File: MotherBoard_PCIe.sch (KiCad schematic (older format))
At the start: 27 parts, among them J1 Conn_01x04, J2 Conn_01x07, J3 Conn_01x04, J4 Conn_01x07, J5 Bus_PCIexpress_x16_164_Positi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, J6 Bus_PCIexpress_x16_164_Positi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, J7 Bus_PCIexpress_x16_164_Positi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

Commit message: buck-up
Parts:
- removed C1: 10uF, Capacitor_SMD:C_1206_3216Metric, symbol Device:C
- removed C10: 1000uF, Capacitor_THT:CP_Radial_D12.5mm_P5.00mm, symbol Device:CP
- removed H5, H6: MountingHole, MountingHole:MountingHole_3.2mm_M3, symbol Mechanical:MountingHole
- removed J1, J3: Conn_01x04, Connector_PinSocket_2.54mm:PinSocket_1x04_P2.54mm_Vertical, symbol Connector_Generic:Conn_01x04
- added C1, C?: 1000uF, Capacitor_THT:CP_Radial_D12.5mm_P5.00mm, symbol Device:CP
- added C10, C?: 10uF, Capacitor_SMD:C_0805_2012Metric, symbol Device:C
- added C?: 1uF, Capacitor_SMD:C_0805_2012Metric, symbol Device:C
- added J1: Conn_01x02, Connector_AMASS:AMASS_XT60-F_1x02_P7.20mm_Vertical, symbol Connector_Generic:Conn_01x02
- added J3: Conn_01x02, Connector_AMASS:AMASS_XT60-M_1x02_P7.20mm_Vertical, symbol Connector_Generic:Conn_01x02
- added J8: Bus_PCIexpress_x16_164_Position, SamacSys_Parts:10018783-10113TLF, symbol SamacSys_Parts:Bus_PCIexpress_x16_164_Position
- added J9: Bus_mechaken_PCIexpress_x16_164_Position, PCIe:Socket_mechaken_PCIexpress_x16_164_position, symbol PCIe:Bus_mechaken_PCIexpress_x16_164_Position
- C11, C12, C6: footprint Capacitor_SMD:C_1206_3216Metric -> Capacitor_SMD:C_0805_2012Metric
- C5, C7, C8, C9: value 0.1uF -> 1uF
- D1: footprint LED_THT:LED_D3.0mm -> LED_THT:LED_D4.0mm
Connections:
- net +5V: now also J8.A1 (Pin_A1), J8.A2 (Pin_A20), J8.B1 (Pin_B1), J8.B2 (Pin_B2), J9.A1 (+5V), J9.B1 (+5V)
- net +BATT: now also J8.A7 (Pin_A7), J8.A8 (Pin_A8), J8.B7 (Pin_B7), J8.B8 (Pin_B8), J9.A5 (+BATT), J9.B5 (+BATT)
- net CANH: now also J8.A6 (Pin_A6), J9.A4 (CANH)
- net CANL: now also J8.A5 (Pin_A5), J9.A3 (CANL)
- net GND: now also J8.A3 (Pin_A3), J8.A4 (Pin_A4), J8.B3 (Pin_B3), J8.B4 (Pin_B4), J9.A2 (GND), J9.B2 (GND)
- net GNDPWR: now also C1.2, C10.2, C?.2, C?.2, C?.2, J1.1 (Pin_1), J3.1 (Pin_1), J8.A14 (Pin_A14), J8.A15 (Pin_A15), J8.A16 (Pin_A16), J8.A17 (Pin_A17), J8.A18 (Pin_A18), J8.A19 (Pin_A19), J8.A20 (Pin_A21), J8.A21 (Pin_A22), J8.A22 (Pin_A23), J8.A53 (Pin_A53), J8.A54 (Pin_A54), J8.A55 (Pin_A55), J8.A56 (Pin_A56), J8.A57 (Pin_A57), J8.A58 (Pin_A58), J8.A59 (Pin_A59), J8.A60 (Pin_A60), J8.A61 (Pin_A61), J8.A62 (Pin_A62), J8.A63 (Pin_A63), J8.A64 (Pin_A64), J8.A65 (Pin_A65), J8.A66 (Pin_A66), J8.A67 (Pin_A67), J8.A68 (Pin_A68), J8.A69 (Pin_A69), J8.A70 (Pin_A70), J8.A71 (Pin_A71), J8.A72 (Pin_A72), J8.A73 (Pin_A73), J8.A74 (Pin_A74), J8.A75 (Pin_A75), J8.A76 (Pin_A76), J8.A77 (Pin_A77), J8.A78 (Pin_A78), J8.A79 (Pin_A79), J8.A80 (Pin_A80), J8.A81 (Pin_A81), J8.A82 (Pin_A82), J8.B14 (Pin_B14), J8.B15 (Pin_B15), J8.B16 (Pin_16), J8.B17 (Pin_B17), J8.B18 (Pin_B18), J8.B19 (Pin_B19), J8.B20 (Pin_B20), J8.B21 (Pin_B21), J8.B22 (Pin_B22), J8.B53 (Pin_B53), J8.B54 (Pin_B54), J8.B55 (Pin_B55), J8.B56 (Pin_B56), J8.B57 (Pin_B57), J8.B58 (Pin_B58), J8.B59 (Pin_B59), J8.B60 (Pin_B60), J8.B61 (Pin_B61), J8.B62 (Pin_B62), J8.B63 (Pin_B63), J8.B64 (Pin_B64), J8.B65 (Pin_B65), J8.B66 (Pin_B66), J8.B67 (Pin_B67), J8.B68 (Pin_B68), J8.B69 (Pin_B69), J8.B70 (Pin_B70), J8.B71 (Pin_B71), J8.B72 (Pin_B72), J8.B73 (Pin_B73), J8.B74 (Pin_B74), J8.B75 (Pin_B75), J8.B76 (Pin_B76), J8.B77 (Pin_B77), J8.B78 (Pin_B78), J8.B79 (Pin_B79), J8.B80 (Pin_B80), J8.B81 (Pin_B81), J8.B82 (Pin_B82), J9.A10 (GNDPWR), J9.A8 (GNDPWR), J9.B10 (GNDPWR), J9.B8 (GNDPWR)
- net Pin_B4: no longer J5.B5 (Pin_B5), J6.B5 (Pin_B5), J7.B5 (Pin_B5)
- net Pin_B5: now also J5.B5 (Pin_B5), J6.B5 (Pin_B5), J7.B5 (Pin_B5), J8.B5 (Pin_B5), J9.B3 (Pin_B5); no longer J5.B6 (Pin_B6), J6.B6 (Pin_B6), J7.B6 (Pin_B6)
- net VCC: now also C1.1, C10.1, C?.1, C?.1, C?.1, J1.2 (Pin_2), J3.2 (Pin_2), J8.A10 (Pin_A10), J8.A11 (Pin_A11), J8.A12 (Pin_A12), J8.A13 (Pin_A13), J8.A23 (Pin_A24), J8.A24 (Pin_A25), J8.A25 (Pin_A26), J8.A26 (Pin_A27), J8.A27 (Pin_A28), J8.A28 (Pin_A28), J8.A29 (Pin_A29), J8.A30 (Pin_A30), J8.A31 (Pin_A31), J8.A32 (Pin_A32), J8.A33 (Pin_A33), J8.A34 (Pin_A34), J8.A35 (Pin_A35), J8.A36 (Pin_A36), J8.A37 (Pin_A37), J8.A38 (Pin_A38), J8.A39 (Pin_A39), J8.A40 (Pin_A40), J8.A41 (Pin_A41), J8.A42 (Pin_A42), J8.A43 (Pin_A43), J8.A44 (Pin_A44), J8.A45 (Pin_A45), J8.A46 (Pin_A46), J8.A47 (Pin_A47), J8.A48 (Pin_A48), J8.A49 (Pin_A49), J8.A50 (Pin_A50), J8.A51 (Pin_A51), J8.A52 (Pin_A52), J8.A9 (Pin_A9), J8.B10 (Pin_B10), J8.B11 (Pin_B11), J8.B12 (Pin_B12), J8.B13 (Pin_B13), J8.B23 (Pin_B23), J8.B24 (Pin_B24), J8.B25 (Pin_B25), J8.B26 (Pin_B26), J8.B27 (Pin_B27), J8.B28 (Pin_B28), J8.B29 (Pin_B29), J8.B30 (Pin_B30), J8.B31 (Pin_B31), J8.B32 (Pin_B32), J8.B33 (Pin_B33), J8.B34 (Pin_B34), J8.B35 (Pin_B35), J8.B36 (Pin_B36), J8.B37 (Pin_B37), J8.B38 (Pin_B38), J8.B39 (Pin_B39), J8.B40 (Pin_B40), J8.B41 (Pin_B41), J8.B42 (Pin_B42), J8.B43 (Pin_B43), J8.B44 (Pin_B44), J8.B45 (Pin_B45), J8.B46 (Pin_B46), J8.B47 (Pin_B47), J8.B48 (Pin_B48), J8.B49 (Pin_B49), J8.B50 (Pin_B50), J8.B51 (Pin_B51), J8.B52 (Pin_B52), J8.B9 (Pin_B9), J9.A6 (VCC), J9.A7 (VCC), J9.A9 (VCC), J9.B6 (VCC), J9.B7 (VCC), J9.B9 (VCC)
- new net Pin_B6: J5.B6 (Pin_B6), J6.B6 (Pin_B6), J7.B6 (Pin_B6), J8.B6 (Pin_B6), J9.B4 (Pin_B6)
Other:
- moved on the sheet: H3

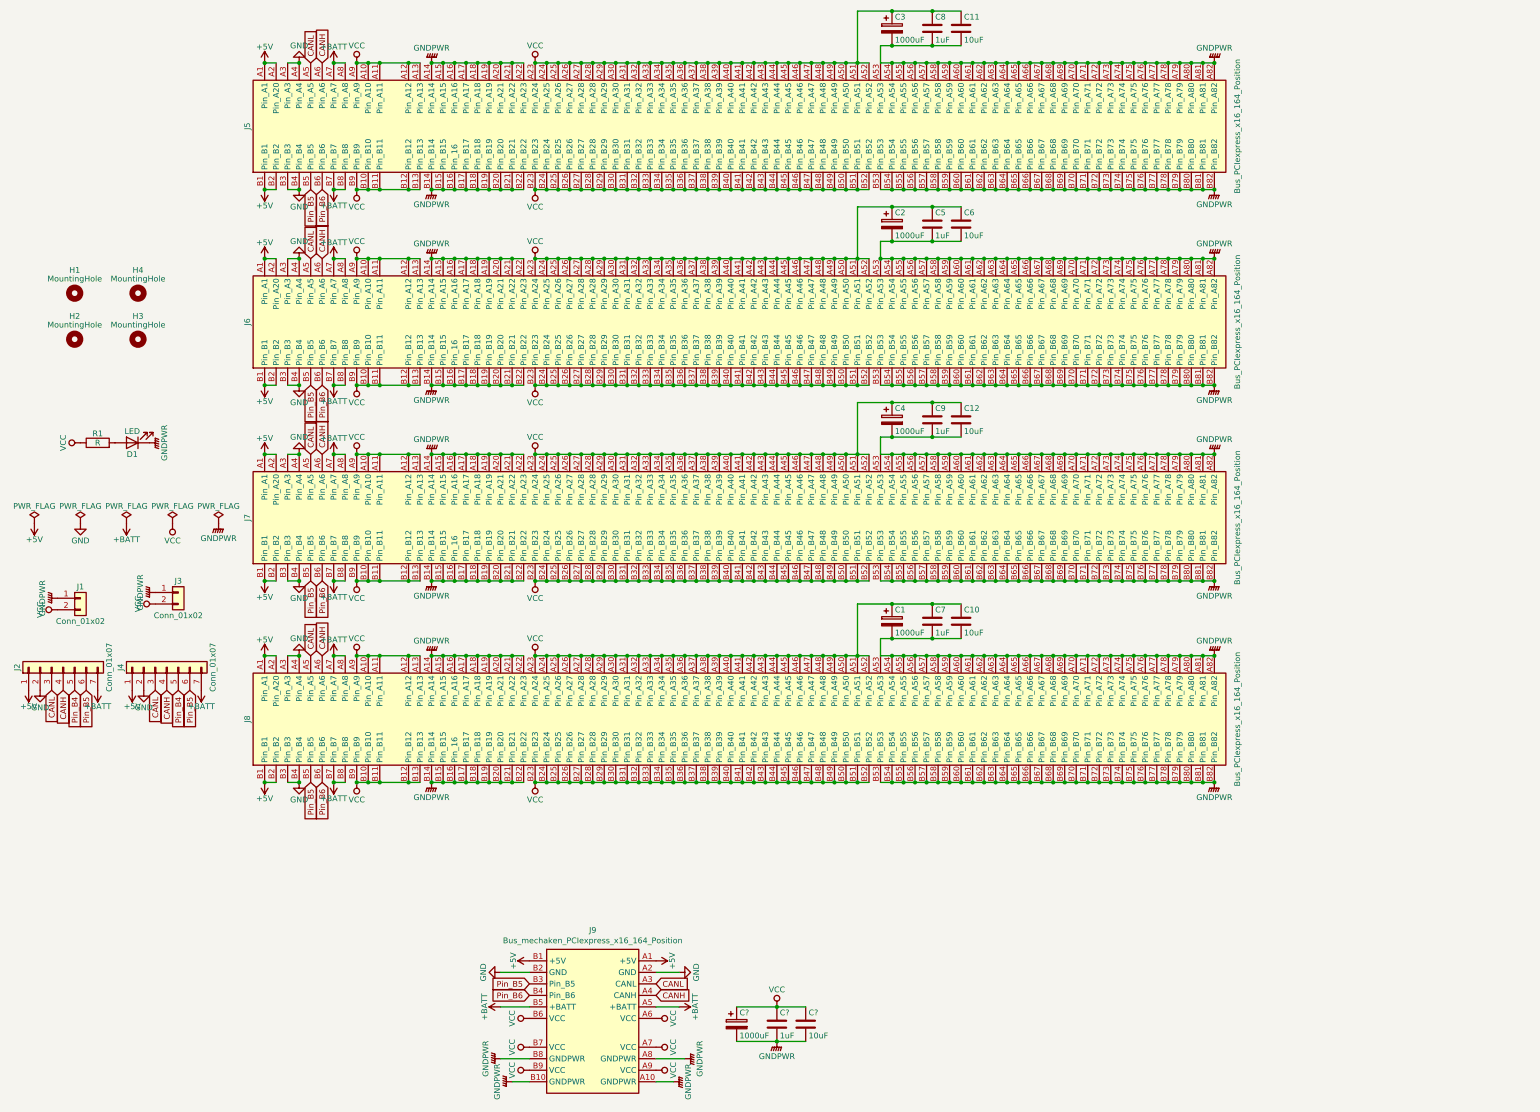
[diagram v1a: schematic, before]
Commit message: change
おおよその部品の配置を開始
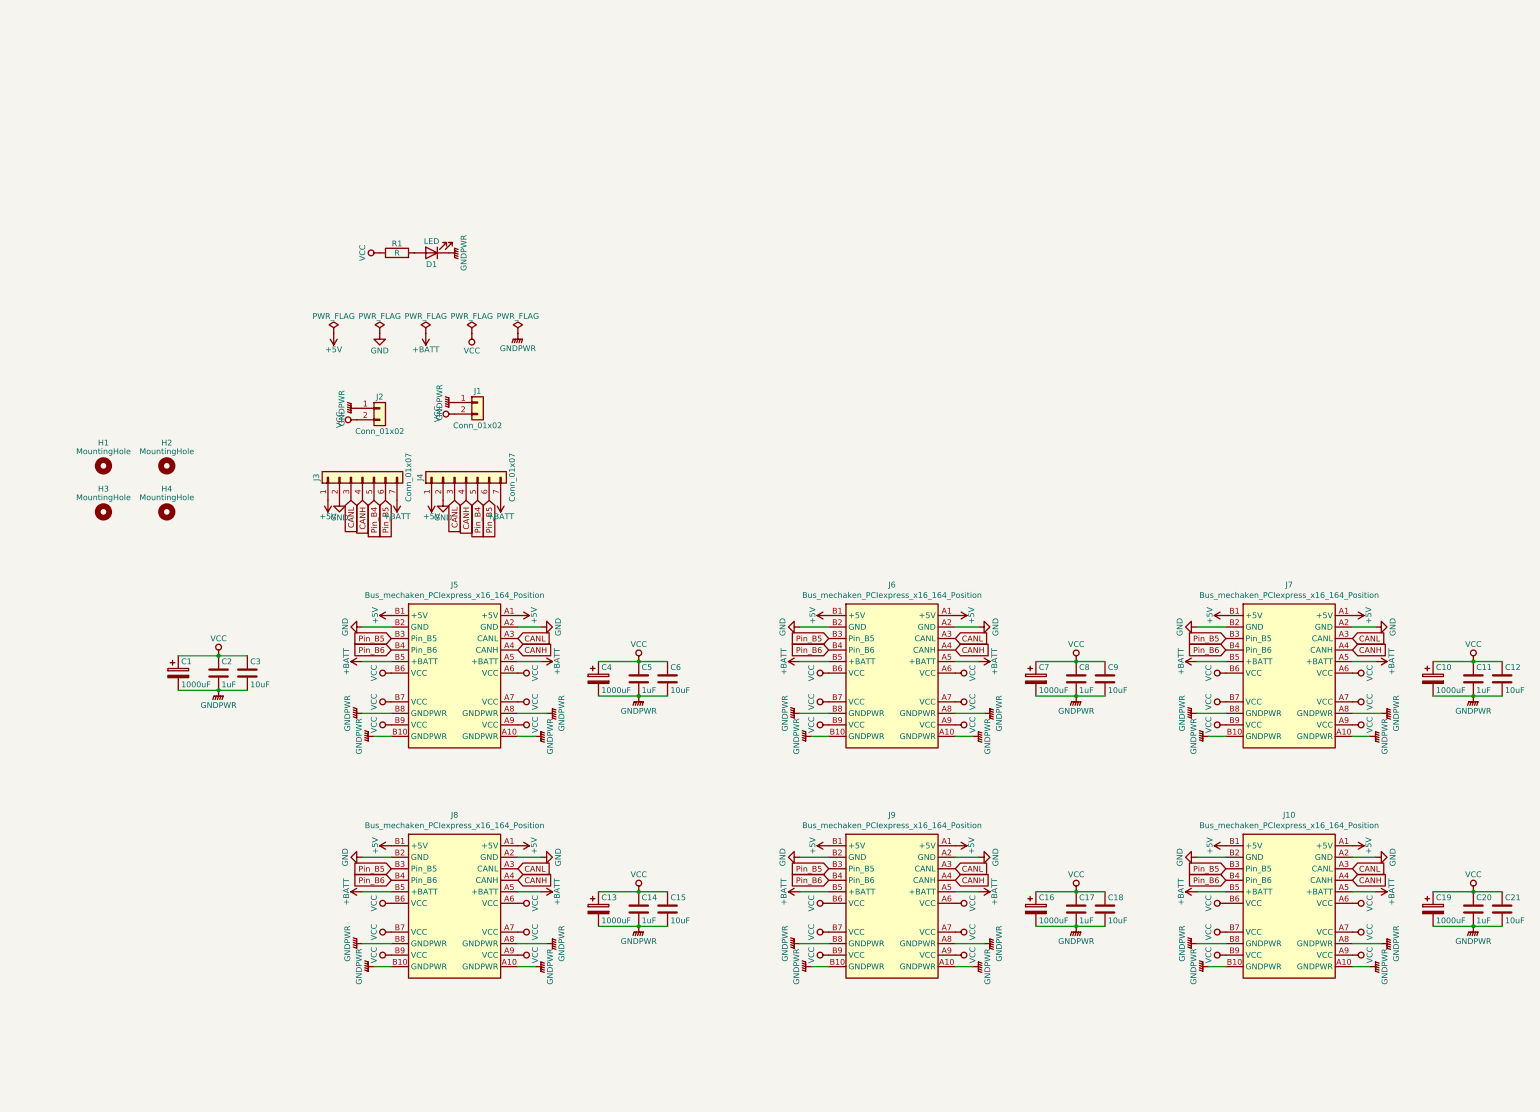
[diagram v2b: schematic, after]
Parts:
- removed C10: 10uF, Capacitor_SMD:C_0805_2012Metric, symbol Device:C
- removed C2, C3: 1000uF, Capacitor_THT:CP_Radial_D12.5mm_P5.00mm, symbol Device:CP
- removed C7, C8, C9: 1uF, Capacitor_SMD:C_0805_2012Metric, symbol Device:C
- removed J5, J6, J7, J8: Bus_PCIexpress_x16_164_Position, SamacSys_Parts:10018783-10113TLF, symbol SamacSys_Parts:Bus_PCIexpress_x16_164_Position
- added C10, C13, C16, C19: 1000uF, Capacitor_THT:CP_Radial_D12.5mm_P5.00mm, symbol Device:CP
- added C14, C17, C2, C20: 1uF, Capacitor_SMD:C_0805_2012Metric, symbol Device:C
- added C15, C18, C21, C3: 10uF, Capacitor_SMD:C_0805_2012Metric, symbol Device:C
- added J10, J5, J7, J8, J9: Bus_mechaken_PCIexpress_x16_164_Position, PCIe:Socket_mechaken_PCIexpress_x16_164_position, symbol PCIe:Bus_mechaken_PCIexpress_x16_164_Position
- C11: value 10uF -> 1uF
- gave numbers to parts that had none: 3
- renumbered H4 to H2, H2 to H3, H3 to H4, J3 to J1, J1 to J2, J2 to J3, J9 to J6
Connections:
- net +5V: now also J10.A1 (+5V), J10.B1 (+5V), J5.A1 (+5V), J5.B1 (+5V), J7.A1 (+5V), J7.B1 (+5V), J8.A1 (+5V), J8.B1 (+5V), J9.A1 (+5V), J9.B1 (+5V)
- net +BATT: now also J10.A5 (+BATT), J10.B5 (+BATT), J5.A5 (+BATT), J5.B5 (+BATT), J7.A5 (+BATT), J7.B5 (+BATT), J8.A5 (+BATT), J8.B5 (+BATT), J9.A5 (+BATT), J9.B5 (+BATT)
- net CANH: now also J10.A4 (CANH), J5.A4 (CANH), J7.A4 (CANH), J8.A4 (CANH), J9.A4 (CANH)
- net CANL: now also J10.A3 (CANL), J5.A3 (CANL), J7.A3 (CANL), J8.A3 (CANL), J9.A3 (CANL)
- net GND: now also J10.A2 (GND), J10.B2 (GND), J5.A2 (GND), J5.B2 (GND), J7.A2 (GND), J7.B2 (GND), J8.A2 (GND), J8.B2 (GND), J9.A2 (GND), J9.B2 (GND)
- net GNDPWR: now also C10.2, C13.2, C14.2, C15.2, C16.2, C17.2, C18.2, C19.2, C2.2, C20.2, C21.2, C3.2, J10.A10 (GNDPWR), J10.A8 (GNDPWR), J10.B10 (GNDPWR), J10.B8 (GNDPWR), J5.A10 (GNDPWR), J5.A8 (GNDPWR), J5.B10 (GNDPWR), J5.B8 (GNDPWR), J7.A10 (GNDPWR), J7.A8 (GNDPWR), J7.B10 (GNDPWR), J7.B8 (GNDPWR), J8.A10 (GNDPWR), J8.A8 (GNDPWR), J8.B10 (GNDPWR), J8.B8 (GNDPWR), J9.A10 (GNDPWR), J9.A8 (GNDPWR), J9.B10 (GNDPWR), J9.B8 (GNDPWR)
- net Pin_B5: now also J10.B3 (Pin_B5), J5.B3 (Pin_B5), J7.B3 (Pin_B5), J8.B3 (Pin_B5), J9.B3 (Pin_B5)
- net Pin_B6: now also J10.B4 (Pin_B6), J5.B4 (Pin_B6), J7.B4 (Pin_B6), J8.B4 (Pin_B6), J9.B4 (Pin_B6)
- net VCC: now also C10.1, C13.1, C14.1, C15.1, C16.1, C17.1, C18.1, C19.1, C2.1, C20.1, C21.1, C3.1, J10.A6 (VCC), J10.A7 (VCC), J10.A9 (VCC), J10.B6 (VCC), J10.B7 (VCC), J10.B9 (VCC), J5.A6 (VCC), J5.A7 (VCC), J5.A9 (VCC), J5.B6 (VCC), J5.B7 (VCC), J5.B9 (VCC), J7.A6 (VCC), J7.A7 (VCC), J7.A9 (VCC), J7.B6 (VCC), J7.B7 (VCC), J7.B9 (VCC), J8.A6 (VCC), J8.A7 (VCC), J8.A9 (VCC), J8.B6 (VCC), J8.B7 (VCC), J8.B9 (VCC), J9.A6 (VCC), J9.A7 (VCC), J9.A9 (VCC), J9.B6 (VCC), J9.B7 (VCC), J9.B9 (VCC)
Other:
- moved on the sheet: C7, C8, C9, D1, H1, H2, H3, H4, J1, J2, J3, J4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

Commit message: add
いったん完成
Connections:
- net Pin_B4 is gone; now on net Pin_B5: J3.5 (Pin_5), J4.5 (Pin_5)
- net GNDPWR: now also R1.2; no longer D1.1 (K)
- net Pin_B5: no longer J3.6 (Pin_6), J4.6 (Pin_6)
- net Pin_B6: now also J3.6 (Pin_6), J4.6 (Pin_6)
- net VCC: now also D1.2 (A); no longer R1.1
- new net: D1.1 (K), R1.1
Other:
- moved on the sheet: D1, R1
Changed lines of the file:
@@
 $EndComp
 Text GLabel 3750 4800 3    50   Input ~ 0
+Pin_B6
+Text GLabel 3650 4800 3    50   Input ~ 0
 Pin_B5
-Text GLabel 3650 4800 3    50   Input ~ 0
-Pin_B4
 $Comp
 L Connector_Generic:Conn_01x07 J4
@@
 $EndComp
 Text GLabel 4650 4800 3    50   Input ~ 0
+Pin_B6
+Text GLabel 4550 4800 3    50   Input ~ 0
 Pin_B5
-Text GLabel 4550 4800 3    50   Input ~ 0
-Pin_B4
 $Comp
 L Device:LED D1
 U 1 1 5DCE8D42
-P 4150 2650
-F 0 "D1" H 4150 2750 50  0000 C CNN
-F 1 "LED" H 4150 2550 50  0000 C CNN
-F 2 "LED_THT:LED_D4.0mm" H 4150 2650 50  0001 C CNN
-F 3 "~" H 4150 2650 50  0001 C CNN
-	1    4150 2650
+P 3850 2650
+F 0 "D1" H 3850 2750 50  0000 C CNN
+F 1 "LED" H 3850 2550 50  0000 C CNN
+F 2 "LED_THT:LED_D4.0mm" H 3850 2650 50  0001 C CNN
+F 3 "~" H 3850 2650 50  0001 C CNN
+	1    3850 2650
 	-1   0    0    1
 $EndComp
@@
 L Device:R R1
 U 1 1 5DCE8D48
-P 3850 2650
-F 0 "R1" V 3930 2650 50  0000 C CNN
-F 1 "R" V 3850 2650 50  0000 C CNN
-F 2 "Resistor_THT:R_Axial_DIN0207_L6.3mm_D2.5mm_P10.16mm_Horizontal" V 3780 2650 50  0001 C CNN
-F 3 "~" H 3850 2650 50  0001 C CNN
-	1    3850 2650
+P 4150 2650
+F 0 "R1" V 4230 2650 50  0000 C CNN
+F 1 "R" V 4150 2650 50  0000 C CNN
+F 2 "Resistor_THT:R_Axial_DIN0207_L6.3mm_D2.5mm_P10.16mm_Horizontal" V 4080 2650 50  0001 C CNN
+F 3 "~" H 4150 2650 50  0001 C CNN
+	1    4150 2650
 	0    -1   -1   0
 $EndComp

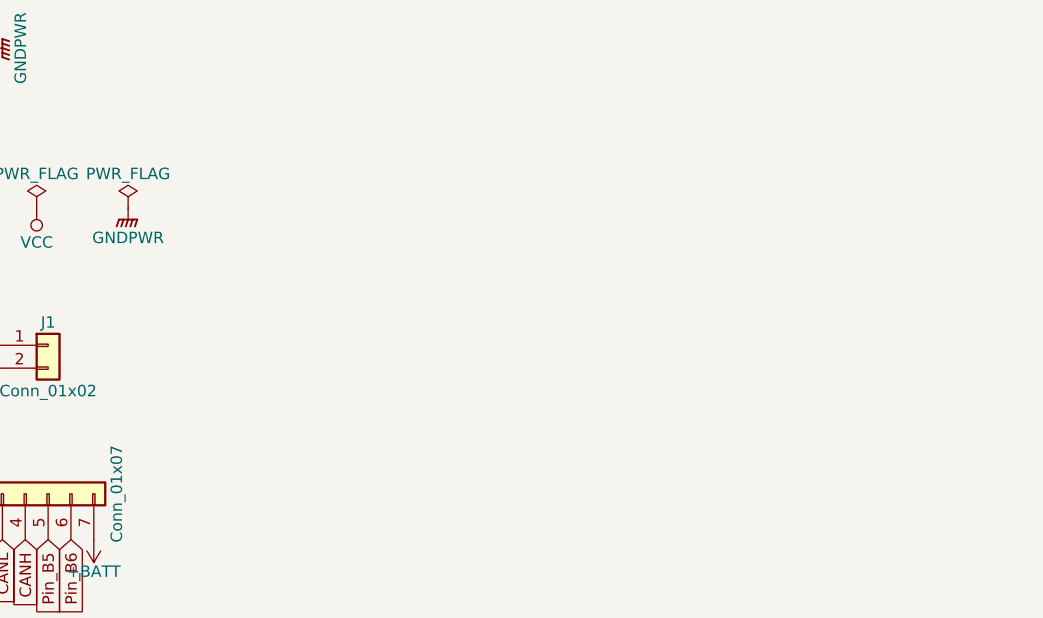
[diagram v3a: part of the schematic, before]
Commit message: add
3ピンファンコネクタを追加
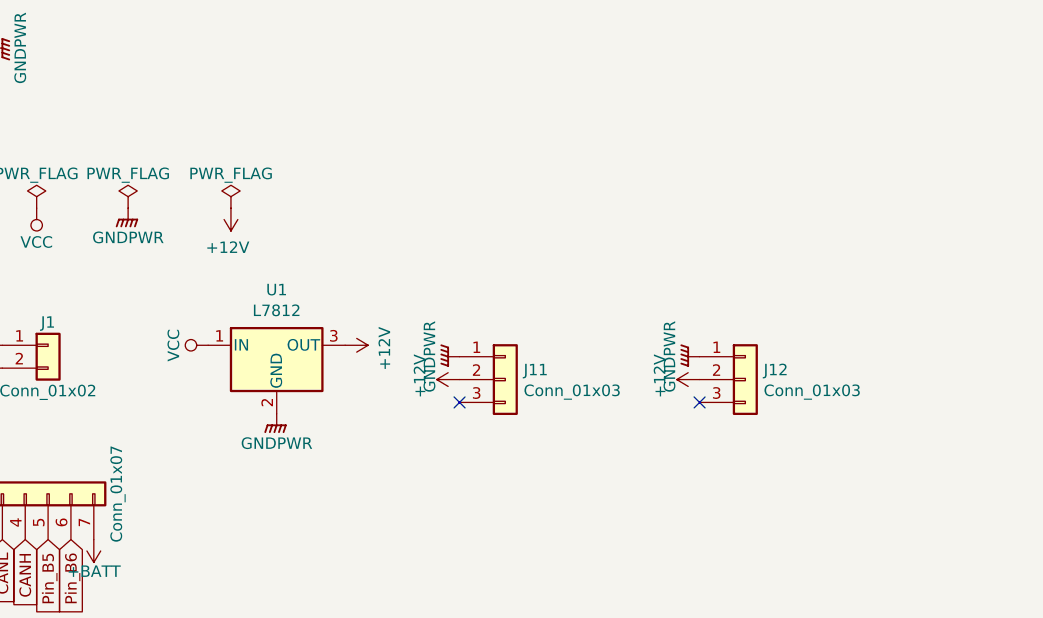
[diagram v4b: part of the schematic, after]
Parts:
- added J11, J12: Conn_01x03, Connector:FanPinHeader_1x03_P2.54mm_Vertical, symbol Connector_Generic:Conn_01x03
- added U1: L7812, Package_TO_SOT_THT:TO-220-3_Vertical, symbol Regulator_Linear:L7812
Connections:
- net GNDPWR: now also J11.1 (Pin_1), J12.1 (Pin_1), U1.2 (GND)
- net VCC: now also U1.1 (IN)
- new net +12V: J11.2 (Pin_2), J12.2 (Pin_2), U1.3 (OUT)
- no-connect marks 0 -> 2
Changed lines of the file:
@@
+	1    0    0    -1
+$EndComp
+$Comp
+L power:+12V #PWR0128
+U 1 1 5E34138A
+P 5350 3350
+F 0 "#PWR0128" H 5350 3200 50  0001 C CNN
+F 1 "+12V" H 5365 3523 50  0000 C CNN
+F 2 "" H 5350 3350 50  0001 C CNN
+F 3 "" H 5350 3350 50  0001 C CNN
+	1    5350 3350
+	-1   0    0    1
+$EndComp
+$Comp
+L power:PWR_FLAG #FLG0101
+U 1 1 5E341DC4
+P 5350 3350
+F 0 "#FLG0101" H 5350 3425 50  0001 C CNN
+F 1 "PWR_FLAG" H 5350 3500 50  0000 C CNN
+F 2 "" H 5350 3350 50  0001 C CNN
+F 3 "~" H 5350 3350 50  0001 C CNN
+	1    5350 3350
+	1    0    0    -1
+$EndComp
+$Comp
+L power:+12V #PWR0129
+U 1 1 5E344D17
+P 5850 3950
+F 0 "#PWR0129" H 5850 3800 50  0001 C CNN
+F 1 "+12V" H 5865 4123 50  0000 C CNN
+F 2 "" H 5850 3950 50  0001 C CNN
+F 3 "" H 5850 3950 50  0001 C CNN
+	1    5850 3950
+	0    1    1    0
+$EndComp
+$Comp
+L power:VCC #PWR0130
+U 1 1 5E347BB0
+P 5250 3950
+F 0 "#PWR0130" H 5250 3800 50  0001 C CNN
+F 1 "VCC" H 5250 4100 50  0000 C CNN
+F 2 "" H 5250 3950 50  0001 C CNN
+F 3 "" H 5250 3950 50  0001 C CNN
+	1    5250 3950
+	0    -1   -1   0
+$EndComp
+$Comp
+L Regulator_Linear:L7812 U1
+U 1 1 5E33E714
+P 5550 3950
+F 0 "U1" H 5550 4192 50  0000 C CNN
+F 1 "L7812" H 5550 4101 50  0000 C CNN
+F 2 "Package_TO_SOT_THT:TO-220-3_Vertical" H 5575 3800 50  0001 L CIN
+F 3 "http://www.st.com/content/ccc/resource/technical/document/datasheet/41/4f/b3/b0/12/d4/47/88/CD00000444.pdf/files/CD00000444.pdf/jcr:content/translations/en.CD00000444.pdf" H 5550 3900 50  0001 C CNN
+	1    5550 3950
+	1    0    0    -1
+$EndComp
+$Comp
+L power:GNDPWR #PWR0131
+U 1 1 5E34AABF
+P 5550 4250
+F 0 "#PWR0131" H 5550 4050 50  0001 C CNN
+F 1 "GNDPWR" H 5550 4120 50  0000 C CNN
+F 2 "" H 5550 4200 50  0001 C CNN
+F 3 "" H 5550 4200 50  0001 C CNN
+	1    5550 4250
+	1    0    0    -1
+$EndComp
+$Comp
+L power:GNDPWR #PWR0132
+U 1 1 5E3746FC
+P 6350 4000
+F 0 "#PWR0132" H 6350 3800 50  0001 C CNN
+F 1 "GNDPWR" H 6350 3870 50  0000 C CNN
+F 2 "" H 6350 3950 50  0001 C CNN
+F 3 "" H 6350 3950 50  0001 C CNN
+	1    6350 4000
+	0    1    1    0
+$EndComp
+NoConn ~ 6350 4200
+$Comp
+L power:+12V #PWR0133
+U 1 1 5E354AFE
+P 6350 4100
+F 0 "#PWR0133" H 6350 3950 50  0001 C CNN
+F 1 "+12V" H 6365 4273 50  0000 C CNN
+F 2 "" H 6350 4100 50  0001 C CNN
+F 3 "" H 6350 4100 50  0001 C CNN
+	1    6350 4100
+	0    -1   -1   0
+$EndComp
+$Comp
+L Connector_Generic:Conn_01x03 J11
+U 1 1 5E33A3AC
+P 6550 4100
+F 0 "J11" H 6630 4142 50  0000 L CNN
+F 1 "Conn_01x03" H 6630 4051 50  0000 L CNN
+F 2 "Connector:FanPinHeader_1x03_P2.54mm_Vertical" H 6550 4100 50  0001 C CNN
+F 3 "~" H 6550 4100 50  0001 C CNN
+	1    6550 4100
+	1    0    0    -1
+$EndComp
+$Comp
+L power:GNDPWR #PWR0134
+U 1 1 5E37C0E3
+P 7400 4000
+F 0 "#PWR0134" H 7400 3800 50  0001 C CNN
+F 1 "GNDPWR" H 7400 3870 50  0000 C CNN
+F 2 "" H 7400 3950 50  0001 C CNN
+F 3 "" H 7400 3950 50  0001 C CNN
+	1    7400 4000
+	0    1    1    0
+$EndComp
+NoConn ~ 7400 4200
+$Comp
+L power:+12V #PWR0135
+U 1 1 5E37C0EA
+P 7400 4100
+F 0 "#PWR0135" H 7400 3950 50  0001 C CNN
+F 1 "+12V" H 7415 4273 50  0000 C CNN
+F 2 "" H 7400 4100 50  0001 C CNN
+F 3 "" H 7400 4100 50  0001 C CNN
+	1    7400 4100
+	0    -1   -1   0
+$EndComp
+$Comp
+L Connector_Generic:Conn_01x03 J12
+U 1 1 5E37C0F0
+P 7600 4100
+F 0 "J12" H 7680 4142 50  0000 L CNN
+F 1 "Conn_01x03" H 7680 4051 50  0000 L CNN
+F 2 "Connector:FanPinHeader_1x03_P2.54mm_Vertical" H 7600 4100 50  0001 C CNN
+F 3 "~" H 7600 4100 50  0001 C CNN
+	1    7600 4100
 	1    0    0    -1
 $EndComp
